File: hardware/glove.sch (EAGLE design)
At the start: 58 parts, among them J1 MICRO_USB_B_JST_MC5BR3-M404-4S, J2 TC2030-JLINK-NL, U1 BNO055, U2 LP3855EMP-ADJ, U3 NRF51822QF, U4 MCP73831, X3 ABS05-32.768KHZ-9-T

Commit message: Worked on the BOM
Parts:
- removed C25: 100 nF, passives:CAPACITOR0402_CAP
- removed C27: 1.0 nF, passives:CAPACITOR0402_CAP
- removed C28: 47 nF, passives:CAPACITOR0402_CAP
- removed C29: 4.7 uF, passives:CAPACITOR0603_CAP
- removed C30: 1.0 uF, passives:CAPACITOR0603_CAP
- removed R17, R18: 10 k, passives:RESISTOR0603_RES
- removed U$1: COMMS, QT1070:COMMS
- added C10, C11, C8, C9: 12 pF, passives:CAPACITOR0402_CAP
- added U5: LP3855EMP-ADJ, LP3855EMP-ADJ:LP3855EMP-ADJ
- C1: value (none) -> 1.0 uF
- C13, C15: device rcl:C-USC0603 -> passives:CAPACITOR0603_CAP
- C14: value 100 nF -> 6.8 nF; device rcl:C-USC0603 -> passives:CAPACITOR0603_CAP
- C16: value 6.8 nF -> 100 nF; device rcl:C-USC0603 -> passives:CAPACITOR0603_CAP
- C17: value 12 pF -> (none); device passives:CAPACITOR0402_CAP -> passives:CAPACITOR0603_CAP
- C18: value 12 pF -> 4.7 uF; device passives:CAPACITOR0402_CAP -> passives:CAPACITOR0603_CAP
- C19: value 12 pF -> 8 nF; device passives:CAPACITOR0402_CAP -> passives:CAPACITOR0603_CAP
- C2: value (none) -> 4.7 uF
- C20: value 12 pF -> 10 uF; device passives:CAPACITOR0402_CAP -> passives:CAPACITOR0603_CAP
- C21: value 2.2 nF -> 4.7 uF; device passives:CAPACITOR0402_CAP -> passives:CAPACITOR0603_CAP
- C22: value 1.0 nF -> 10 uF; device passives:CAPACITOR0402_CAP -> passives:CAPACITOR0603_CAP
- C3: value (none) -> 100 nF; device passives:CAPACITOR0603_CAP -> passives:CAPACITOR0402_CAP
- C4: value (none) -> 1.0 nF; device passives:CAPACITOR0603_CAP -> passives:CAPACITOR0402_CAP
- C5: value 8 nF -> 47 nF; device passives:CAPACITOR0603_CAP -> passives:CAPACITOR0402_CAP
- C6: value 10 uF -> 1.0 nF; device passives:CAPACITOR0603_CAP -> passives:CAPACITOR0402_CAP
- C7: value 10 uF -> 2.2 nF; device passives:CAPACITOR0603_CAP -> passives:CAPACITOR0402_CAP
- J1: value MICRO_USB_B_JST_MC5BR3-M404-4S -> TC2030-JLINK-NL; device connector:MICRO_USB_B_JST_MC5BR3-M404-4S -> connector:TC2030-JLINK-NL
- J2: value TC2030-JLINK-NL -> MICRO_USB_B_JST_MC5BR3-M404-4S; device connector:TC2030-JLINK-NL -> connector:MICRO_USB_B_JST_MC5BR3-M404-4S
- R1, R3: value 10 K -> 1 k; device rcl:R-US_R0603 -> passives:RESISTOR0603_RES
- R10, R11, R6: value (none) -> 10 k
- R12: value 440 -> 10 k
- R13: value 250 -> 470
- R14: value 1k -> 250
- R15: value 10 k -> 440
- R16: value 10 k -> 2 k
- R2: value 10 K -> 150; device rcl:R-US_R0603 -> passives:RESISTOR0603_RES
- R4: value (none) -> 1 k
- R5: value (none) -> 12 k
- R8: value (none) -> 47 k
- R9: value 47 k -> 10 k
- U1: value BNO055 -> NRF51822QF; device BNO055:BNO055 -> chips:NRF51822QF
- U2: value LP3855EMP-ADJ -> BNO055; device LP3855EMP-ADJ:LP3855EMP-ADJ -> BNO055:BNO055
- U3: value NRF51822QF -> AT42QT1070; device chips:NRF51822QF -> QT1070:AT42QT1070
- renumbered C24 to C12, L10 to L2, L9 to L1, X3 to X1
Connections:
- removed net SLCK: U3.P09
- removed net VDD: C14.1, C15.1, C16.1, R1.2, R2.2, R3.2, U1.VDD, U1.VDDIO
- net FLEX0: now also U1.P01/AIN2; no longer U3.P01/AIN2
- net FLEX1: now also U1.P02/AIN3; no longer U3.P02/AIN3
- net FLEX2: now also U1.P03/AIN4; no longer U3.P03/AIN4
- net FLEX3: now also U1.P04/AIN5; no longer U3.P04/AIN5
- net GND: now also C10.2, C11.2, C22.1, C5.2, C6.2, C8.2, C9.2, R14.2, R16.1, R2.1, U1.GND, U2.COM3, U2.PS0, U2.PS1, U3.MODE, U3.VSS, U5.GND; no longer C19.2, C22.2, C25.2, C27.2, C28.2, C29.2, C30.2, C6.1, R13.2, R4.1, R7.1, U$1.MODE, U$1.VSS, U1.COM3, U1.PS0, U1.PS1, U2.GND, U3.GND
- net GNDIO: now also U2.COM2, U2.GND, U2.GNDIO, U2.PIN10, U2.PIN15, U2.PIN16; no longer U1.COM2, U1.GND, U1.GNDIO, U1.PIN10, U1.PIN15, U1.PIN16
- net INT: now also U2.INT; no longer U1.INT
- net N$1: now also C21.1; no longer C2.1, C3.1
- net N$14: now also U1.DCC; no longer U3.DCC
- net N$16: now also C1.1, C4.1, U1.AVDD; no longer C27.1, C30.1, U3.AVDD
- net N$17: now also R8.1, U3.!CHANGE; no longer R9.1, U$1.!CHANGE
- net N$18: now also R6.1, U2.NBOOT_LOAD_PIN; no longer R3.1, U1.NBOOT_LOAD_PIN
- net N$19: now also J1.SWDIO, R2.2, U1.SWDIO/!RESET; no longer J2.SWDIO, R4.2, U3.SWDIO/!RESET
- net N$2: now also LED2.ANODE, R13.1; no longer LED1.ANODE, R6.1
- net N$20: now also C11.1, U1.XC2; no longer C20.1, U3.XC2
- net N$21: now also U1.ANT1; no longer U3.ANT1
- net N$22: now also U1.ANT2; no longer U3.ANT2
- net N$23: now also C7.1, U1.VDD_PA; no longer C21.1, U3.VDD_PA
- net N$25: now also C5.1, U1.DEC2; no longer C28.1, U3.DEC2
- net N$26: now also C6.1, U1.DEC1; no longer C22.1, U3.DEC1
- net N$27: now also C8.1, U1.P26/AIN0/XL2; no longer C17.1, U3.P26/AIN0/XL2
- net N$28: now also C9.1, U1.P27/AIN1/XL1; no longer C18.1, U3.P27/AIN1/XL1
- net N$29: now also C10.1, U1.XC1; no longer C19.1, U3.XC1
- net N$3: now also LED2.CATHODE; no longer LED1.CATHODE
- net N$30: now also J1.SWDCLK, U1.SWDCLK; no longer J2.SWDCLK, U3.SWDCLK
- net N$31: now also R11.2, U3.KEY3; no longer R15.2, U$1.KEY3
- net N$32: now also R11.1; no longer R15.1
- net N$33: now also R9.2, U3.KEY2; no longer R16.2, U$1.KEY2
- net N$34: now also R9.1; no longer R16.1
- net N$35: now also R12.2, U3.KEY1; no longer R17.2, U$1.KEY1
- net N$36: now also R12.1; no longer R17.1
- net N$37: now also R10.2, U3.KEY0; no longer R18.2, U$1.KEY0
- net N$38: now also C18.1, J2.+5V, R13.2; no longer C1.1, J1.+5V, R6.2
- net N$39: now also R10.1; no longer R18.1
- net N$4: now also R16.2; no longer R7.2
- net N$40: now also R7.1, U3.!RESET; no longer R8.1, U$1.!RESET
- net N$5: now also C22.2, U5.VIN; no longer C6.2, U2.VIN
- net N$6: now also LED1.CATHODE, U1.P13; no longer LED2.CATHODE, U3.P13
- net N$7: now also C19.1, R14.1, R15.2, U5.ADJ; no longer C5.1, R12.2, R13.1, U2.ADJ
- net N$8: now also LED1.ANODE, R1.1; no longer LED2.ANODE, R14.1
- net N$9: now also U2.CAP; no longer U1.CAP
- net SCL: now also R3.1, U1.P07, U2.COM1, U3.SCL; no longer R1.1, R11.1, U$1.SCL, U1.COM1, U3.P07
- net SDA: now also R4.1, U1.P08, U2.COM0, U3.SDA; no longer R10.1, R2.1, U$1.SDA, U1.COM0, U3.P08
- net VCC: now also C14.1, C15.1, C16.1, C17.1, C19.2, C2.1, C20.1, C3.1, J1.VCC, R1.2, R15.1, R3.2, R4.2, R6.2, R7.2, U1.VDD, U2.VDD, U2.VDDIO, U5.VOUT; no longer C25.1, C29.1, C4.1, C5.2, C7.1, J2.VCC, R10.2, R11.2, R12.1, R14.2, R9.2, U$1.VDD, U2.VOUT
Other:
- note added: "Input Capacitance: 5-10pF"

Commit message: Started work on BOM
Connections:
- net N$5: now also U5.~SD
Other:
- note added: "<1cm away from device"
- note added: "Ceramic"
- note added: "Tantalum"
- note added: "Tantalum/Ceramic"
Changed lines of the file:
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@@
 <sheet>
 <plain>
+<text x="134.62" y="-35.56" size="1.778" layer="91">Ceramic</text>
 </plain>
 <instances>
@@
 <sheet>
 <plain>
+<text x="60.96" y="-15.24" size="1.778" layer="91">Tantalum/Ceramic</text>
+<text x="0" y="-27.94" size="1.778" layer="91">&lt;1cm away from device</text>
+<text x="5.08" y="-30.48" size="1.778" layer="91">Tantalum</text>
 </plain>
 <instances>
@@
 <wire x1="104.14" y1="-17.78" x2="55.88" y2="-17.78" width="0.1524" layer="91"/>
 <pinref part="C22" gate="G$1" pin="2"/>
-<wire x1="55.88" y1="-17.78" x2="48.26" y2="-17.78" width="0.1524" layer="91"/>
+<wire x1="55.88" y1="-17.78" x2="50.8" y2="-17.78" width="0.1524" layer="91"/>
 <junction x="55.88" y="-17.78"/>
-</segment>
-</net>
+<pinref part="U5" gate="A" pin="~SD"/>
+<wire x1="50.8" y1="-17.78" x2="48.26" y2="-17.78" width="0.1524" layer="91"/>
+<wire x1="48.26" y1="-12.7" x2="50.8" y2="-12.7" width="0.1524" layer="91"/>
+<wire x1="50.8" y1="-12.7" x2="50.8" y2="-17.78" width="0.1524" layer="91"/>
+<junction x="50.8" y="-17.78"/>
+</segment>
+</net>

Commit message: It's a board
We got this
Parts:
- removed LED1: LED0603, leds:LED0603
- added D1, D10, D11, D12, D2, D3, D4, D5, D6, D7, D8, D9: 1N4004, diode:1N4004
- added LED12, LED13, LED14, LED15: LED0603, leds:LED0603
- added PAD1, PAD10, PAD11, PAD12, PAD13, PAD14, PAD15, PAD2, PAD3, PAD4, PAD5, PAD6, PAD7, PAD8, PAD9: WIREPAD1,6/0,8, wirepad:WIREPAD1,6/0,8
- added R17, R18, R19: 1 k, passives:RESISTOR0603_RES
- added R20, R21, R22, R23: (no value), passives:RESISTOR0603_RES
- renumbered LED2 to CHG
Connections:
- new net HEART: PAD3.P, U1.P05/AIN6
- new net N$10: LED15.CATHODE, U1.P15
- new net N$11: LED15.ANODE, R17.1
- new net N$12: LED12.CATHODE, U1.P12
- new net N$13: LED12.ANODE, R18.1
- new net N$41: D4.C, PAD6.P
- new net N$42: LED13.ANODE, R19.1
- new net N$43: LED13.CATHODE, U1.P13
- new net N$44: D1.C, PAD4.P
- new net N$45: D2.A, PAD5.P
- new net N$46: D2.C, D3.A
- new net N$47: D5.A, PAD7.P
- new net N$48: D5.C, D6.A
- new net N$49: D7.C, PAD8.P
- new net N$50: D8.A, PAD9.P
- new net N$51: D8.C, D9.A
- new net N$52: D10.C, PAD10.P
- new net N$53: D11.A, PAD11.P
- new net N$54: D11.C, D12.A
- net FLEX0: now also D3.C, R20.1
- net FLEX1: now also D6.C, R21.1
- net FLEX2: now also D9.C, R22.1
- net FLEX3: now also D12.C, R23.1
- net GND: now also PAD2.P, R20.2, R21.2, R22.2, R23.2
- net N$32: now also PAD12.P
- net N$34: now also PAD13.P
- net N$36: now also PAD14.P
- net N$39: now also PAD15.P
- net N$6: now also LED14.CATHODE, U1.P14; no longer LED1.CATHODE, U1.P13
- net N$8: now also LED14.ANODE; no longer LED1.ANODE
- net VCC: now also D1.A, D10.A, D4.A, D7.A, PAD1.P, R17.2, R18.2, R19.2

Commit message: lol haf done boardl
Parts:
- removed D1, D10, D11, D12, D2, D3, D4, D5, D6, D7, D8, D9: 1N4004, diode:1N4004
- added C23: 1uF, passives:CAPACITOR0603_CAP
- added R24: 100k, passives:RESISTOR0603_RES
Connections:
- removed net N$44: D1.C, PAD4.P
- removed net N$45: D2.A, PAD5.P
- removed net N$46: D2.C, D3.A
- removed net N$47: D5.A, PAD7.P
- removed net N$48: D5.C, D6.A
- removed net N$49: D7.C, PAD8.P
- removed net N$50: D8.A, PAD9.P
- removed net N$51: D8.C, D9.A
- removed net N$52: D10.C, PAD10.P
- removed net N$53: D11.A, PAD11.P
- removed net N$54: D11.C, D12.A
- net FLEX0: now also PAD5.P; no longer D3.C
- net FLEX1: now also PAD7.P; no longer D6.C
- net FLEX2: now also PAD9.P; no longer D9.C
- net FLEX3: now also PAD11.P; no longer D12.C
- net GND: now also C23.1, R24.1
- net N$1: no longer SW11.P, SW12.P
- net N$38: now also R24.2
- net N$41: now also C23.2, SW11.P, SW12.P; no longer D4.C, PAD6.P
- net VCC: now also PAD10.P, PAD4.P, PAD6.P, PAD8.P; no longer D1.A, D10.A, D4.A, D7.A
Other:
- note added: "B130LAW"
- note added: "DMP1045U"
- moved on the sheet: SW11, SW12

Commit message: 54 wires left! (woo?)
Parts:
- added D1: B130LAW, load_balance:B130LAW
- added P1: DMP1045U, load_balance:DMP1045U
- PAD1, PAD10, PAD11, PAD2, PAD3, PAD4, PAD5, PAD6, PAD7, PAD8, PAD9: value WIREPAD1,6/0,8 -> WIREPAD1,6/0,9; device wirepad:WIREPAD1,6/0,8 -> wirepad:WIREPAD1,6/0,9
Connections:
- net N$1: now also C23.2, D1.OUT, P1.SOURCE, SW11.P, SW12.P; no longer C21.1, CN1.2, U4.VBAT
- net N$38: now also D1.IN, P1.GATE
- net N$41: now also C21.1, CN1.2, P1.DRAIN, U4.VBAT; no longer C23.2, SW11.P, SW12.P
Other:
- note removed: "B130LAW"
- note removed: "DMP1045U"
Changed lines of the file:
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@@
 <part name="LED13" library="leds" deviceset="LED" device="0603"/>
 <part name="R19" library="passives" deviceset="RESISTOR" device="0603_RES" value="1 k"/>
-<part name="PAD3" library="wirepad" deviceset="WIREPAD" device="1,6/0,8"/>
-<part name="PAD4" library="wirepad" deviceset="WIREPAD" device="1,6/0,8"/>
-<part name="PAD5" library="wirepad" deviceset="WIREPAD" device="1,6/0,8"/>
-<part name="PAD2" library="wirepad" deviceset="WIREPAD" device="1,6/0,8"/>
-<part name="PAD1" library="wirepad" deviceset="WIREPAD" device="1,6/0,8"/>
+<part name="PAD3" library="wirepad" deviceset="WIREPAD" device="1,6/0,9" value="WIREPAD1,6/0,9"/>
+<part name="PAD4" library="wirepad" deviceset="WIREPAD" device="1,6/0,9" value="WIREPAD1,6/0,9"/>
+<part name="PAD5" library="wirepad" deviceset="WIREPAD" device="1,6/0,9" value="WIREPAD1,6/0,9"/>
+<part name="PAD2" library="wirepad" deviceset="WIREPAD" device="1,6/0,9" value="WIREPAD1,6/0,9"/>
+<part name="PAD1" library="wirepad" deviceset="WIREPAD" device="1,6/0,9" value="WIREPAD1,6/0,9"/>
 <part name="P+2" library="supply1" deviceset="VCC" device=""/>
 <part name="GND20" library="supply1" deviceset="GND" device=""/>
@@
 <part name="GND21" library="supply1" deviceset="GND" device=""/>
 <part name="P+8" library="supply1" deviceset="VCC" device=""/>
-<part name="PAD6" library="wirepad" deviceset="WIREPAD" device="1,6/0,8"/>
-<part name="PAD7" library="wirepad" deviceset="WIREPAD" device="1,6/0,8"/>
+<part name="PAD6" library="wirepad" deviceset="WIREPAD" device="1,6/0,9" value="WIREPAD1,6/0,9"/>
+<part name="PAD7" library="wirepad" deviceset="WIREPAD" device="1,6/0,9" value="WIREPAD1,6/0,9"/>
 <part name="R21" library="passives" deviceset="RESISTOR" device="0603_RES"/>
 <part name="GND22" library="supply1" deviceset="GND" device=""/>
 <part name="P+9" library="supply1" deviceset="VCC" device=""/>
-<part name="PAD8" library="wirepad" deviceset="WIREPAD" device="1,6/0,8"/>
-<part name="PAD9" library="wirepad" deviceset="WIREPAD" device="1,6/0,8"/>
+<part name="PAD8" library="wirepad" deviceset="WIREPAD" device="1,6/0,9" value="WIREPAD1,6/0,9"/>
+<part name="PAD9" library="wirepad" deviceset="WIREPAD" device="1,6/0,9" value="WIREPAD1,6/0,9"/>
 <part name="R22" library="passives" deviceset="RESISTOR" device="0603_RES"/>
 <part name="GND23" library="supply1" deviceset="GND" device=""/>
 <part name="P+10" library="supply1" deviceset="VCC" device=""/>
-<part name="PAD10" library="wirepad" deviceset="WIREPAD" device="1,6/0,8"/>
-<part name="PAD11" library="wirepad" deviceset="WIREPAD" device="1,6/0,8"/>
+<part name="PAD10" library="wirepad" deviceset="WIREPAD" device="1,6/0,9" value="WIREPAD1,6/0,9"/>
+<part name="PAD11" library="wirepad" deviceset="WIREPAD" device="1,6/0,9" value="WIREPAD1,6/0,9"/>
 <part name="R23" library="passives" deviceset="RESISTOR" device="0603_RES"/>
 <part name="GND24" library="supply1" deviceset="GND" device=""/>
@@
 <part name="GND25" library="supply1" deviceset="GND" device=""/>
 <part name="R24" library="passives" deviceset="RESISTOR" device="0603_RES" value="100k"/>
+<part name="P1" library="load_balance" deviceset="DMP1045U" device=""/>
+<part name="D1" library="load_balance" deviceset="B130LAW" device=""/>
 </parts>
 <sheets>
@@
 <text x="0" y="-27.94" size="1.778" layer="91">&lt;1cm away from device</text>
 <text x="5.08" y="-30.48" size="1.778" layer="91">Tantalum</text>
-<text x="79.756" y="27.432" size="1.778" layer="91">B130LAW</text>
-<text x="60.96" y="22.86" size="1.778" layer="91">DMP1045U</text>
 </plain>
 <instances>
@@
 <instance part="GND25" gate="1" x="111.76" y="40.64" rot="R180"/>
 <instance part="R24" gate="G$1" x="91.44" y="33.02" rot="R180"/>
+<instance part="P1" gate="G$1" x="60.96" y="25.4" rot="MR270"/>
+<instance part="D1" gate="G$1" x="83.82" y="17.78" rot="R270"/>
 </instances>
 <busses>
@@
 <junction x="-50.8" y="20.32"/>
 <wire x1="-40.64" y1="20.32" x2="-40.64" y2="33.02" width="0.1524" layer="91"/>
-<wire x1="-40.64" y1="33.02" x2="83.82" y2="33.02" width="0.1524" layer="91"/>
+<pinref part="P1" gate="G$1" pin="GATE"/>
+<wire x1="-40.64" y1="33.02" x2="60.96" y2="33.02" width="0.1524" layer="91"/>
 <pinref part="R24" gate="G$1" pin="2"/>
 <wire x1="83.82" y1="33.02" x2="88.9" y2="33.02" width="0.1524" layer="91"/>
 <wire x1="83.82" y1="33.02" x2="83.82" y2="30.48" width="0.1524" layer="91"/>
+<pinref part="D1" gate="G$1" pin="IN"/>
+<wire x1="60.96" y1="33.02" x2="83.82" y2="33.02" width="0.1524" layer="91"/>
+<junction x="60.96" y="33.02"/>
 <junction x="83.82" y="33.02"/>
 </segment>
@@
 <net name="N$1" class="0">
 <segment>
-<pinref part="C21" gate="G$1" pin="1"/>
-<pinref part="U4" gate="G$1" pin="VBAT"/>
-<wire x1="12.7" y1="20.32" x2="40.64" y2="20.32" width="0.1524" layer="91"/>
-<wire x1="40.64" y1="20.32" x2="40.64" y2="17.78" width="0.1524" layer="91"/>
-<junction x="40.64" y="20.32"/>
-<wire x1="40.64" y1="20.32" x2="55.88" y2="20.32" width="0.1524" layer="91"/>
-<pinref part="CN1" gate="G$1" pin="2"/>
-<wire x1="68.58" y1="15.24" x2="55.88" y2="15.24" width="0.1524" layer="91"/>
-<wire x1="55.88" y1="15.24" x2="55.88" y2="20.32" width="0.1524" layer="91"/>
-<junction x="55.88" y="20.32"/>
-<wire x1="55.88" y1="22.86" x2="55.88" y2="20.32" width="0.1524" layer="91"/>
-<wire x1="55.88" y1="22.86" x2="58.42" y2="22.86" width="0.1524" layer="91"/>
+<pinref part="D1" gate="G$1" pin="OUT"/>
+<wire x1="76.2" y1="15.24" x2="83.82" y2="15.24" width="0.1524" layer="91"/>
+<wire x1="83.82" y1="15.24" x2="101.6" y2="15.24" width="0.1524" layer="91"/>
+<junction x="83.82" y="15.24"/>
+<pinref part="SW1" gate="2" pin="P"/>
+<pinref part="SW1" gate="1" pin="P"/>
+<wire x1="114.3" y1="22.86" x2="114.3" y2="7.62" width="0.1524" layer="91"/>
+<pinref part="C23" gate="G$1" pin="2"/>
+<wire x1="114.3" y1="22.86" x2="101.6" y2="22.86" width="0.1524" layer="91"/>
+<junction x="114.3" y="22.86"/>
+<wire x1="101.6" y1="15.24" x2="101.6" y2="22.86" width="0.1524" layer="91"/>
+<junction x="101.6" y="22.86"/>
+<pinref part="P1" gate="G$1" pin="SOURCE"/>
+<wire x1="71.12" y1="20.32" x2="76.2" y2="20.32" width="0.1524" layer="91"/>
+<wire x1="76.2" y1="20.32" x2="76.2" y2="15.24" width="0.1524" layer="91"/>
 </segment>
 </net>
@@
 <net name="N$41" class="0">
 <segment>
-<pinref part="SW1" gate="2" pin="P"/>
-<pinref part="SW1" gate="1" pin="P"/>
-<wire x1="114.3" y1="22.86" x2="114.3" y2="7.62" width="0.1524" layer="91"/>
-<pinref part="C23" gate="G$1" pin="2"/>
-<wire x1="114.3" y1="22.86" x2="101.6" y2="22.86" width="0.1524" layer="91"/>
-<junction x="114.3" y="22.86"/>
-<wire x1="73.66" y1="22.86" x2="83.82" y2="22.86" width="0.1524" layer="91"/>
-<junction x="101.6" y="22.86"/>
-<wire x1="83.82" y1="22.86" x2="101.6" y2="22.86" width="0.1524" layer="91"/>
-<wire x1="83.82" y1="22.86" x2="83.82" y2="25.4" width="0.1524" layer="91"/>
-<junction x="83.82" y="22.86"/>
-</segment>
-</net>
+<pinref part="C21" gate="G$1" pin="1"/>
+<wire x1="40.64" y1="20.32" x2="40.64" y2="17.78" width="0.1524" layer="91"/>
+<pinref part="U4" gate="G$1" pin="VBAT"/>
+<wire x1="12.7" y1="20.32" x2="40.64" y2="20.32" width="0.1524" layer="91"/>
+<pinref part="P1" gate="G$1" pin="DRAIN"/>
+<wire x1="40.64" y1="20.32" x2="48.26" y2="20.32" width="0.1524" layer="91"/>
+<junction x="40.64" y="20.32"/>
+<wire x1="48.26" y1="20.32" x2="50.8" y2="20.32" width="0.1524" layer="91"/>
+<wire x1="48.26" y1="20.32" x2="48.26" y2="15.24" width="0.1524" layer="91"/>
+<junction x="48.26" y="20.32"/>
+<pinref part="CN1" gate="G$1" pin="2"/>
+<wire x1="68.58" y1="15.24" x2="48.26" y2="15.24" width="0.1524" layer="91"/>
+</segment>
+</net>

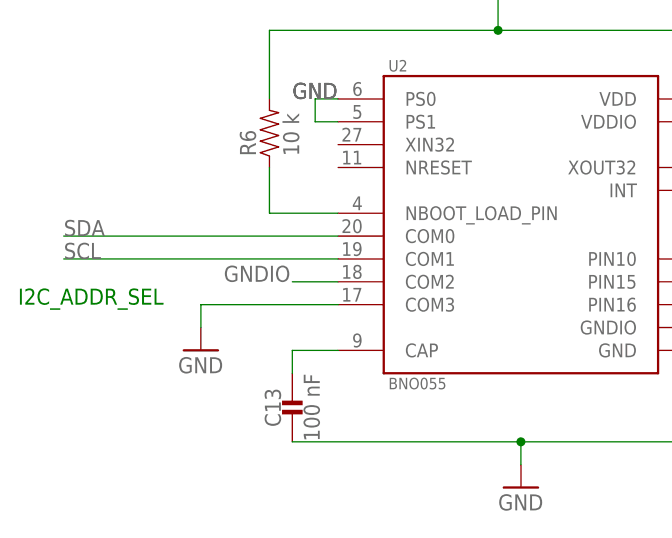
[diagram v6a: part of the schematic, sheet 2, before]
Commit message: Completely routed!
Some final layout tweaks needed, but everything is connected and it looks like it works
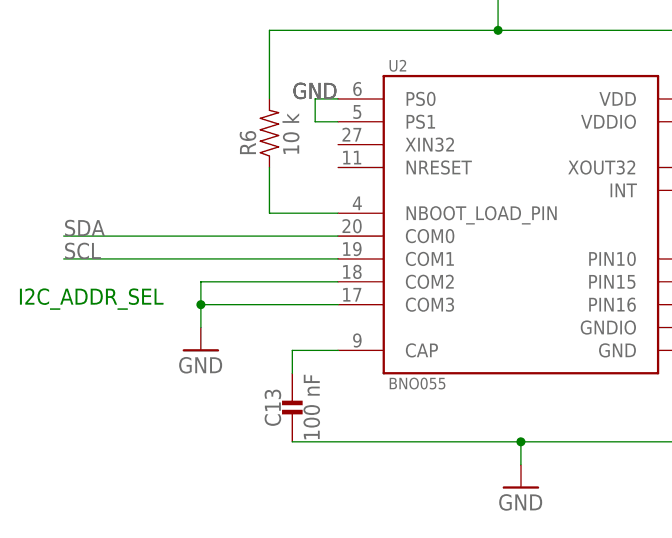
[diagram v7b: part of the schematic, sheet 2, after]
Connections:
- removed net GNDIO: C13.2, C14.2, C15.2, C16.2, U2.COM2, U2.GND, U2.GNDIO, U2.PIN10, U2.PIN15, U2.PIN16
- net GND: now also C13.2, C14.2, C15.2, C16.2, U2.COM2, U2.GND, U2.GNDIO, U2.PIN10, U2.PIN15, U2.PIN16
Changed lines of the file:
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@@
 <?xml version="1.0" encoding="utf-8"?>
 <!DOCTYPE eagle SYSTEM "eagle.dtd">
-<eagle version="7.7.0">
+<eagle version="7.6.0">
 <drawing>
 <settings>
@@
 <pinref part="GND15" gate="1" pin="GND"/>
 <wire x1="-35.56" y1="-12.7" x2="-35.56" y2="-10.16" width="0.1524" layer="91"/>
-</segment>
-</net>
-<net name="GNDIO" class="0">
+<pinref part="U2" gate="G$1" pin="COM2"/>
+<wire x1="-20.32" y1="-7.62" x2="-35.56" y2="-7.62" width="0.1524" layer="91"/>
+<wire x1="-35.56" y1="-7.62" x2="-35.56" y2="-10.16" width="0.1524" layer="91"/>
+<junction x="-35.56" y="-10.16"/>
+</segment>
 <segment>
 <pinref part="GND16" gate="1" pin="GND"/>
@@
 <junction x="33.02" y="-12.7"/>
 </segment>
-<segment>
-<pinref part="U2" gate="G$1" pin="COM2"/>
-<wire x1="-20.32" y1="-7.62" x2="-25.4" y2="-7.62" width="0.1524" layer="91"/>
-<label x="-33.02" y="-7.62" size="1.778" layer="95"/>
-</segment>
-</net>
+</net>
